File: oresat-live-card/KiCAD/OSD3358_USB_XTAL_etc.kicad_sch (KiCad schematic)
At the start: 81 parts, among them J10 SM06B-SRSS-TB(LF)(SN), J2 SM06B-SRSS-TB(LF)(SN), U1 RCLAMP0504FB, U2 TUSB4020BI, U20 TPS2041BQDBVRQ1, U7 OSD3358-512M-BSM, U9 TPS2041BQDBVRQ1, Y1 24MHz, Y2 ABS07-32.768KHZ-T, Y3 24MHz

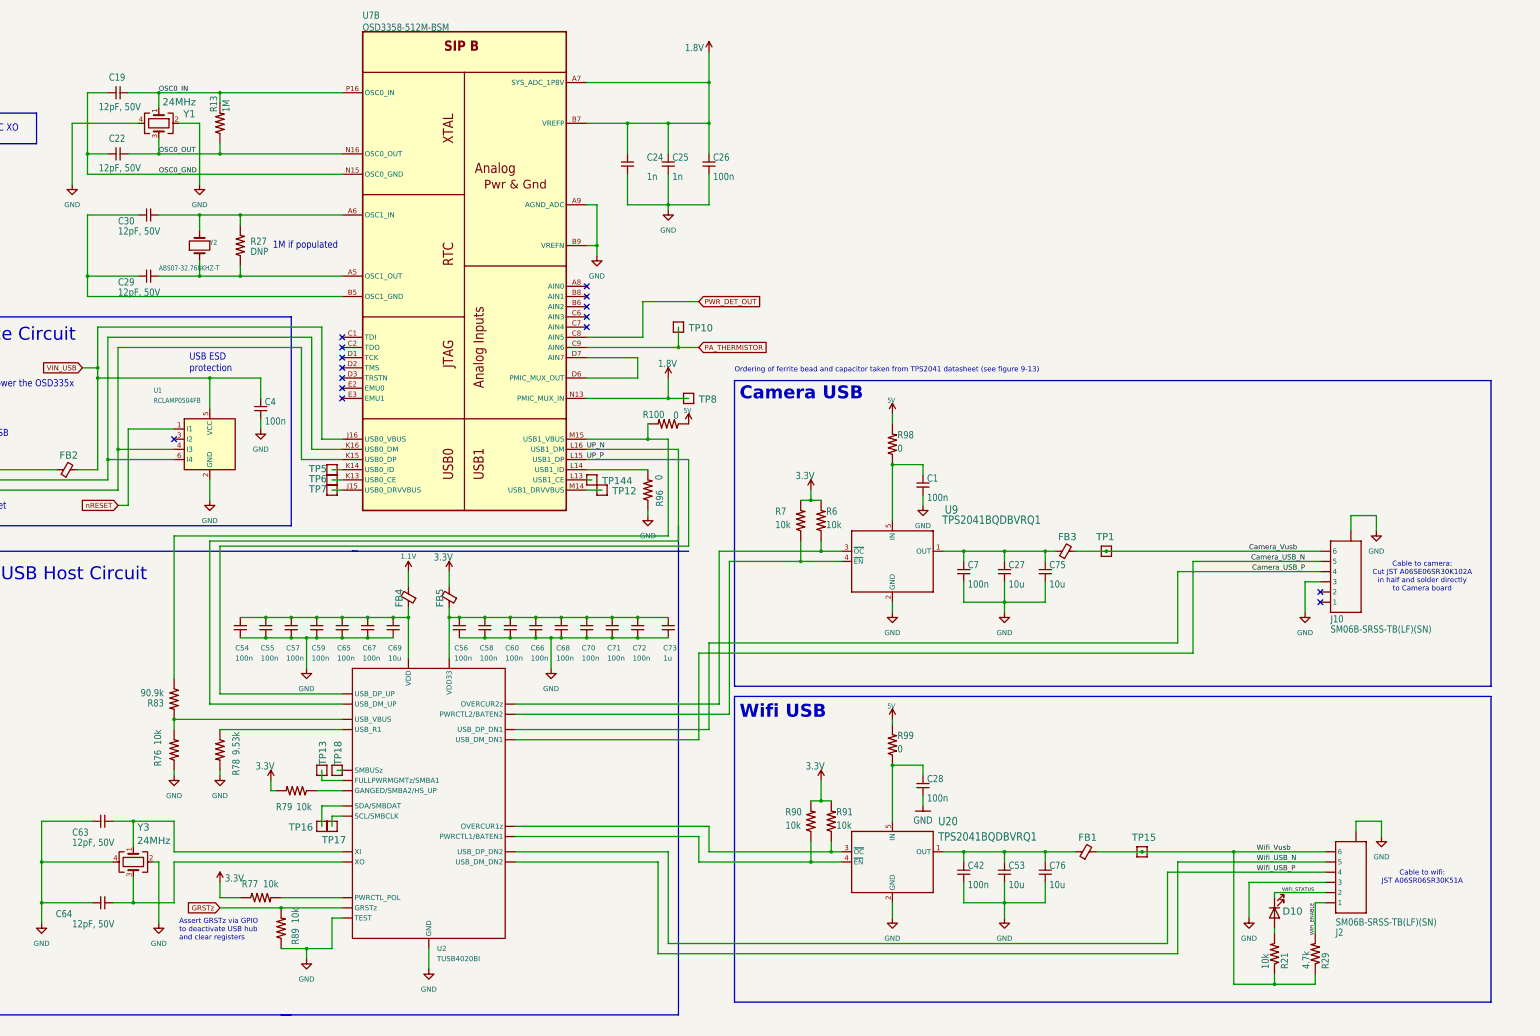
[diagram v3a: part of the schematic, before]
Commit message: Fixed up schematic as best as possible. There were a lot of issues with local paths being referenced, and EAGLE import libraries. Fixed all of those, as well as fixed some oresat-kicad IC symbols (bad direction pins) and I think we're now OK. Also updated card outline for two RF (LEFT) connectors.  Still missing two packages, but we'll deal with that later.
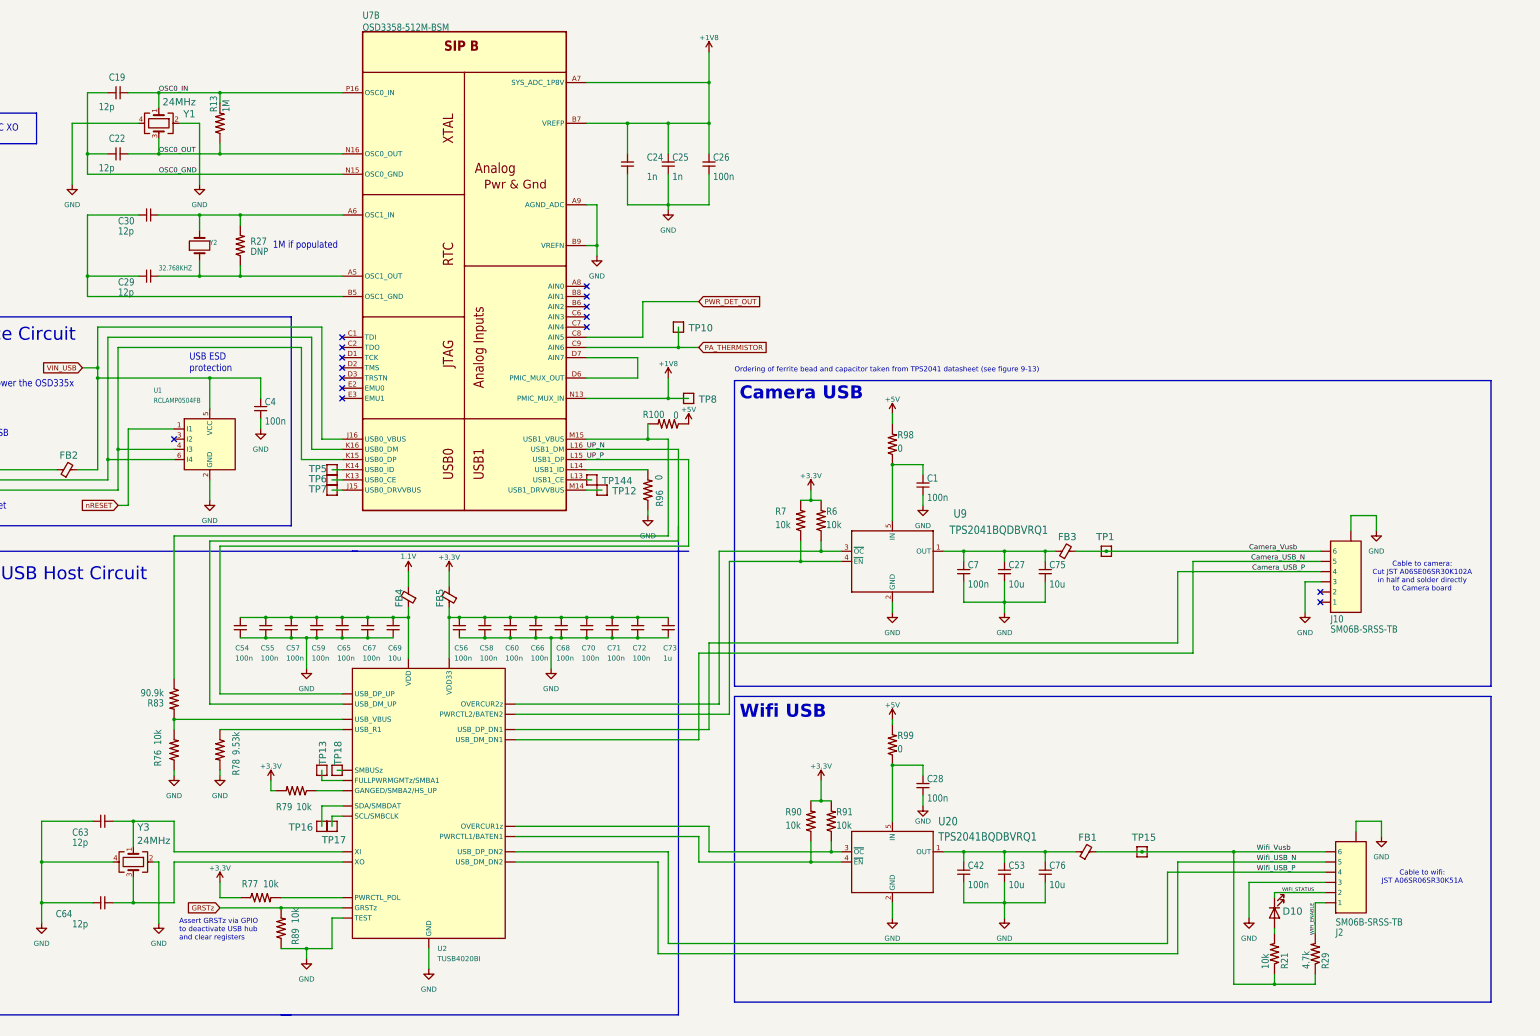
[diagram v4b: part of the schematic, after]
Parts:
- C1, C28, C4, C42, C54, C55, C56, C57, C58, C59, C60, C65, C66, C67, C68, C7, C70, C71, C72: DPN (none) -> 445-5667-1-ND; MFR (none) -> TDK Corporation; MPN CL10B104KB8WPNC -> CGA3E2X7R1E104K080AA
- C19, C22, C29, C30, C63, C64: value 12pF, 50V -> 12p; DPN (none) -> 445-5629-1-ND; MFR (none) -> TDK Corporation; MPN 06035C120J4T2A -> CGA3E2C0G1H120J080AA
- C24, C25: DPN (none) -> 445-173649-1-ND; MFR (none) -> TDK Corporation; MPN C0805F102K1RACAUTO -> CGA4F2X7R2A102K085AE
- C26: DPN (none) -> 445-15959-1-ND; MFR (none) -> TDK Corporation; MPN CL21B104KBF5PNE -> CGA4J2X7R1H104K125AE
- C27, C53, C69, C75, C76: DPN (none) -> 445-16111-1-ND; MFR (none) -> TDK Corporation; MPN CGA4J1X7R0J106M125AC -> CGA4J1X7S1C106M125AC
- C73: DPN (none) -> 445-12539-1-ND; MFR (none) -> TDK Corporation; MPN CGA3E1X7R1E105M080AE -> CGA3E1X7R1C105K080AC
- D10: value 150060VS55040 -> GREEN; DPN (none) -> 732-150060GS75020CT-ND; MFR (none) -> Würth Elektronik
- FB1, FB2, FB3: value BLM18KG300JH1D -> BLM18KG300TH1D; DPN (none) -> 490-13263-1-ND; MFR (none) -> Murata Electronics
- FB4, FB5: value BLM18KG300JH1D -> MMZ1608Y221BTD25; DPN (none) -> 445-MMZ1608Y221BTD25CT-ND; MFR (none) -> TDK Corporation
- J10, J2: value SM06B-SRSS-TB(LF)(SN) -> SM06B-SRSS-TB; DPN (none) -> 306-M06BSRSSTBLFSNPP; Distributor DigiKey -> Mouser; MFR (none) -> JST Commercial
- R100, R96, R98, R99: DPN (none) -> P0.0GCT-ND; MFR (none) -> Panasonic; MPN ERJ-3EKF1002V -> ERJ-3GEY0R00V
- R13: DPN (none) -> P1.00MHCT-ND; MFR (none) -> Panasonic
- R21, R6, R7, R76, R77, R79, R89, R90, R91: DPN (none) -> P10.0KHCT-ND; MFR (none) -> Panasonic
- R29: DPN (none) -> ERJ-3EKF4701V; MFR (none) -> Panasonic
- R78: DPN (none) -> P9.53KHCT-ND; MFR (none) -> Panasonic; MPN RMCF0603FT9K53 -> ERJ-3EKF9531V
- R83: DPN (none) -> P90.9KHCT-ND; MFR (none) -> Panasonic
- U1: DPN (none) -> RCLAMP0504FBTCTCT-ND; MFR (none) -> Semtech Corporation
- U2: DPN (none) -> 296-43165-1-ND; MFR (none) -> Texas Instruments
- U20, U9: DPN (none) -> 296-25159-1-ND; MFR (none) -> Texas Instruments; MPN TPS2041BQDBVRQ1 -> TPS2041BQDBVRQ1
- U7: DPN (none) -> 1676-1002-ND; MFR (none) -> Octavo Systems
- Y1, Y3: DPN (none) -> XC2580CT-ND; MFR (none) -> ECS Inc.; MPN ECS-240-20-30B-TR -> ECS-240-20ECS-240-12-30BQ-AEN-TR -30B-TR
- Y2: value ABS07-32.768KHZ-T -> 32.768KHZ; DPN (none) -> 535-9542-1-ND; MFR (none) -> Abracon LLC
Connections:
- net 1.8V renamed +1V8
- net 3.3V renamed +3.3V
- net 5V renamed +5V

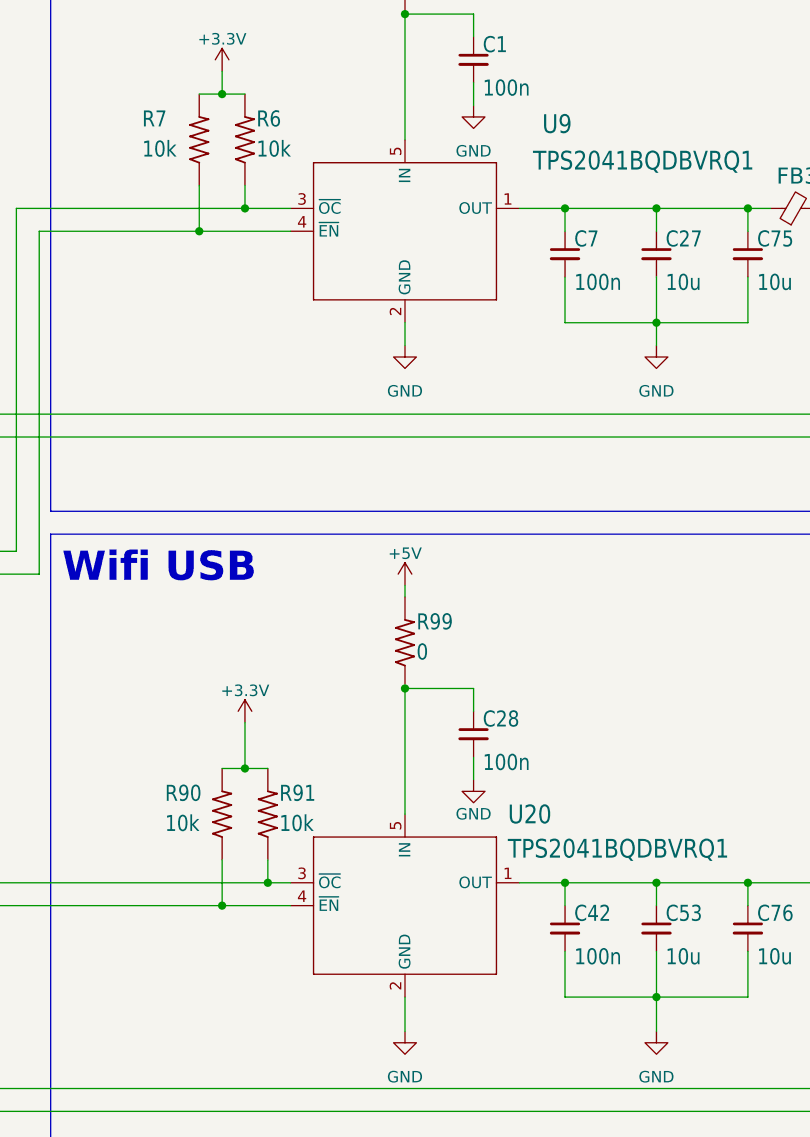
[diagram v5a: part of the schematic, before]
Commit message: fixed USB hub symbol to be filled
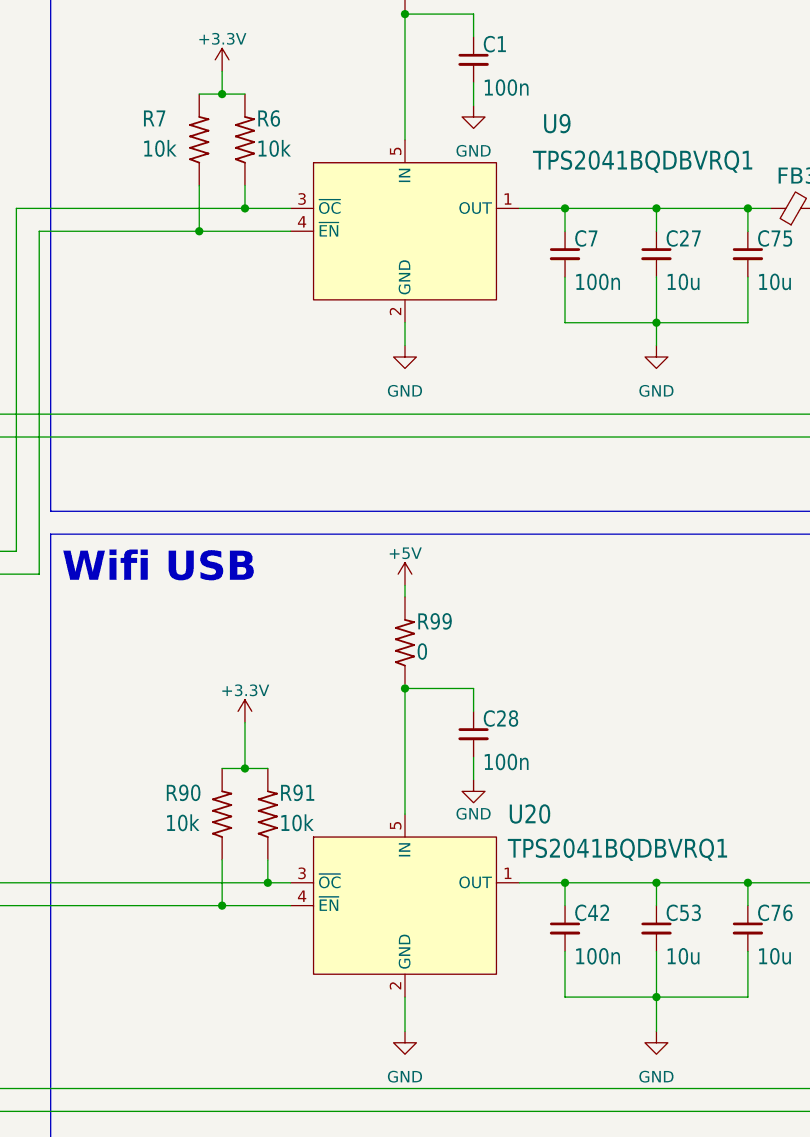
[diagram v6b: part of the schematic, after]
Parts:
- U20, U9: MPN TPS2041BQDBVRQ1 -> TPS2041BQDBVRQ1
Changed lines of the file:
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@@
 	)
 	(symbol
+		(lib_name "TPS2041BQDBVRQ1_1")
 		(lib_id "oresat-ics:TPS2041BQDBVRQ1")
 		(at 264.16 148.59 0)
@@
 			)
 		)
-		(property "Description" "IC PWR SWITCH N-CHAN 1:1 SOT23-5"
+		(property "Description" "Power Switch/Driver 1:1 N-Channel 500mA"
 			(at 264.16 148.59 0)
 			(effects
@@
 			)
 		)
-		(property "MPN" "TPS2041BQDBVRQ1 "
+		(property "MPN" "TPS2041BQDBVRQ1"
 			(at 264.16 148.59 0)
 			(effects
@@
 			)
 		)
-		(property "Description" "IC PWR SWITCH N-CHAN 1:1 SOT23-5"
+		(property "Description" "Power Switch/Driver 1:1 N-Channel 500mA"
 			(at 264.16 223.52 0)
 			(effects
@@
 			)
 		)
-		(property "MPN" "TPS2041BQDBVRQ1 "
+		(property "MPN" "TPS2041BQDBVRQ1"
 			(at 264.16 223.52 0)
 			(effects

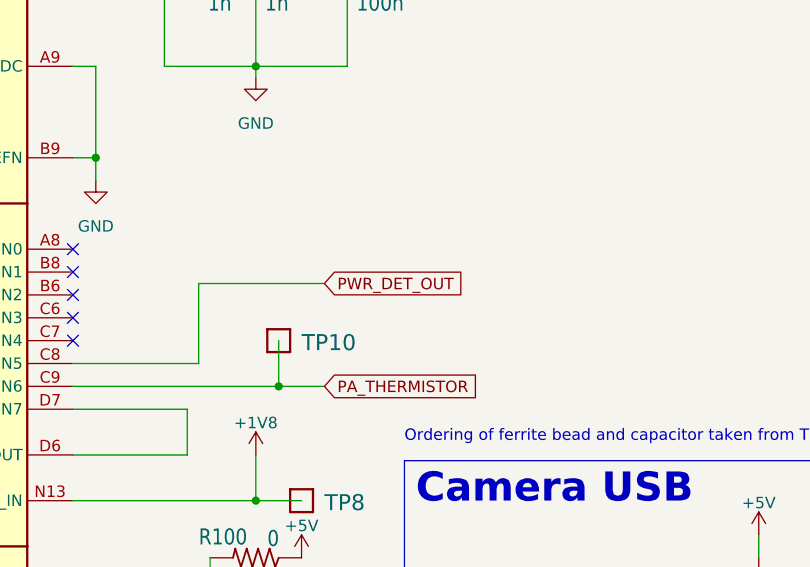
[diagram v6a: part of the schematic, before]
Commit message: swapped placement of R105 and R88, changed R109 from 100 to 56 ohms, relabelled PWR_DET_OUT to RX_DET_OUT, added inverter to TX/RX Control switch and swapped RF1 and RF2
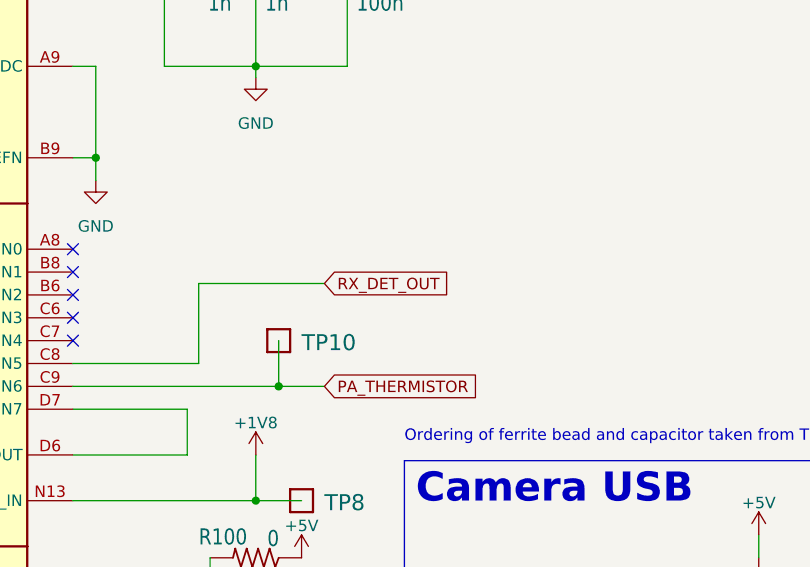
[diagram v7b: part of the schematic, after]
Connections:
- net PWR_DET_OUT renamed RX_DET_OUT
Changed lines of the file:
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@@
 		)
 	)
-	(global_label "PWR_DET_OUT"
+	(global_label "RX_DET_OUT"
 		(shape input)
 		(at 215.9 86.36 0)
@@
 		)
 		(property "Intersheetrefs" "${INTERSHEET_REFS}"
-			(at 231.827 86.36 0)
+			(at 230.3151 86.36 0)
 			(effects
 				(font
